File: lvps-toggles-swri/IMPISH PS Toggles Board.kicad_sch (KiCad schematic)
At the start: 0 parts

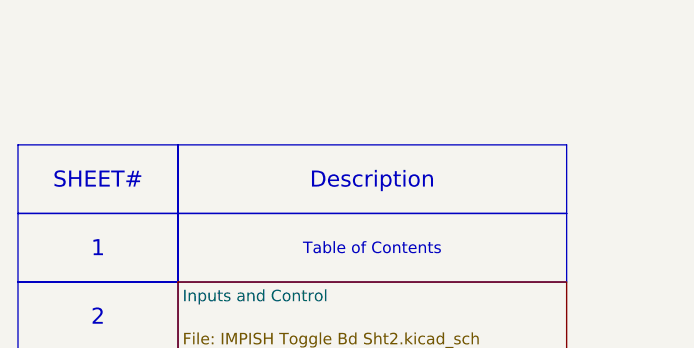
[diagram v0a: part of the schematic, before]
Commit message: Power board updates (#7)
* toggles adapter board

The SwRI toggle output is in the wrong direction,
so we are adding an additional PCB to point the power
towards the side of the EPS box. We can route it with
cables and connectors instead of using the board-to-board
style interface.

* toggles adapter: cleanup

* toggles adapter: via stitching

* swri toggles: start one ground

* swri toggles: single ground pre stitching

* swri toggles: via stitching for gnd

* swri toggles: fix DRC and ERC errors

* swri lvps main: two layer board

* swri lvps main: fix cap models
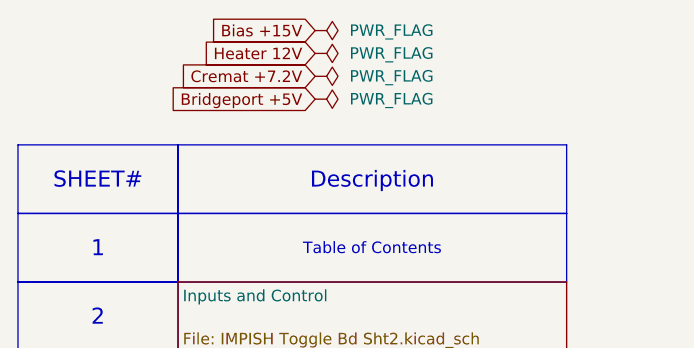
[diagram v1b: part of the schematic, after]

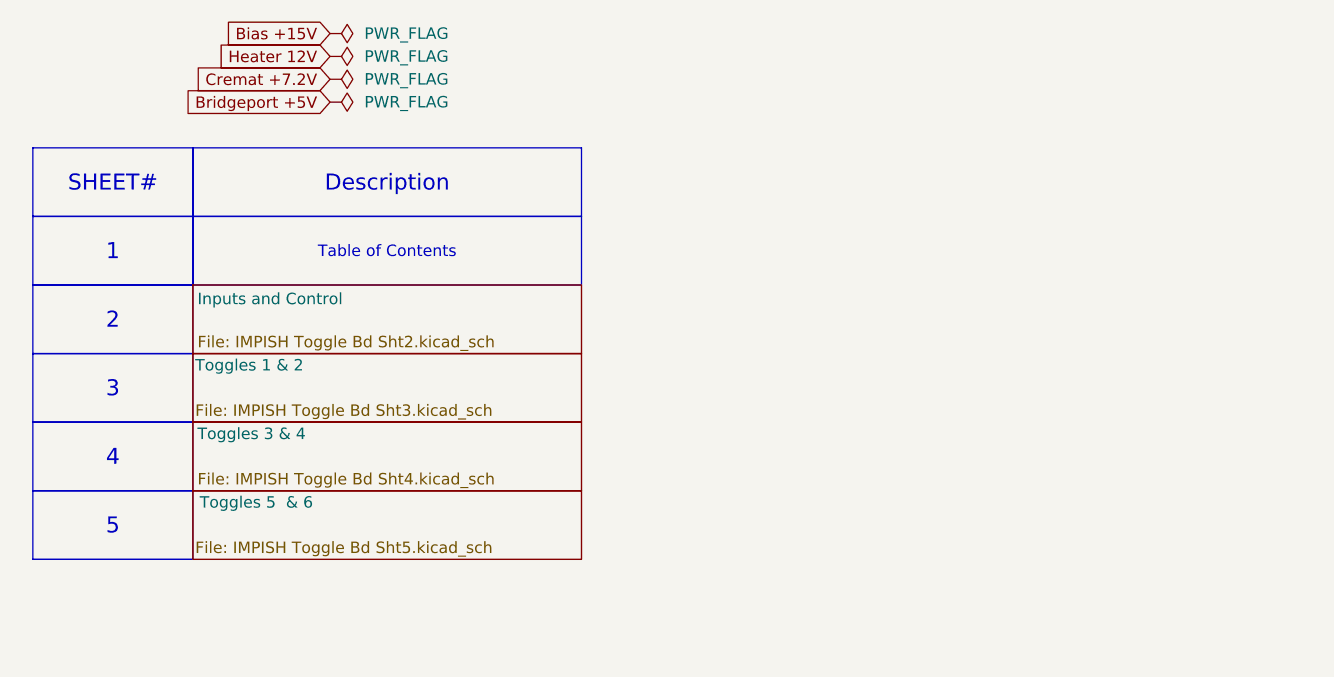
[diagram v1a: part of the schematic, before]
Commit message: toggles
remove cremat, fix layout, add DAQBOX toggle/power line
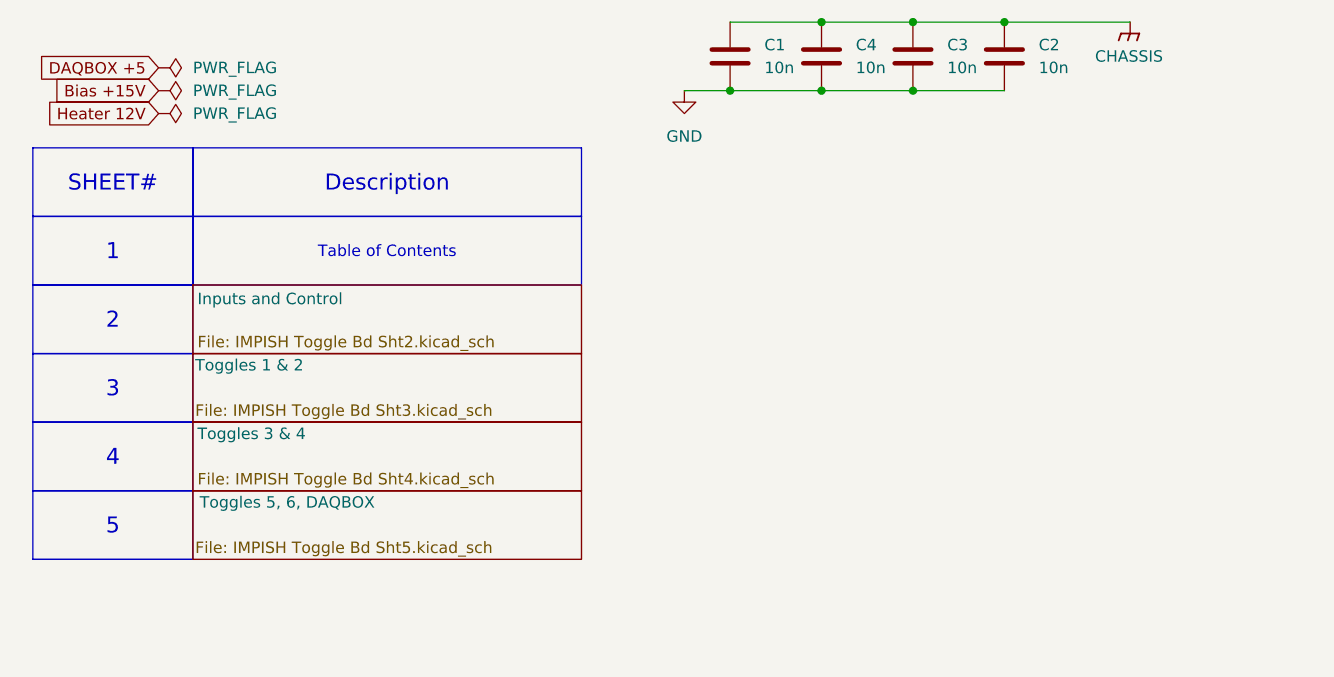
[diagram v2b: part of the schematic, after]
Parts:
- added C1, C2, C3, C4: 10n, Capacitor_SMD:C_0805_2012Metric_Pad1.18x1.45mm_HandSolder, symbol Device:C
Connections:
- new net CHASSIS: C1.1, C2.1, C3.1, C4.1
- new net GND: C1.2, C2.2, C3.2, C4.2
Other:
- sheet Toggles 5  & 6 renamed Toggles 5, 6, DAQBOX
